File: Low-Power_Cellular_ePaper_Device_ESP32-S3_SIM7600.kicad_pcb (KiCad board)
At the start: 4 copper layers, 85 x 57.5 mm, 100 parts, among them J1 USB_C_Receptacle_GCT_USB4085, J2 JST_PH_S2B-PH-K_1x02_P2.00mm_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, J3 nanoSIM_GCT_SIM8060-6-0-14-00, J4 U.FL_Hirose_U.FL-R-SMT-1_Vert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, J5 U.FL_Hirose_U.FL-R-SMT-1_Vert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, J6 Hirose_FH12-24S-0.5SH_1x24-1M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, J7 JST_SH_SM04B-SRSS-TB_1x04-1MP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, Q1 SOT-23, Q10 SOT-23, Q2 SOT-23, Q3 SOT-23, Q4 SOT-23, Q6 SOT-23, Q7 SOT-23, Q8 SOT-23, Q9 SOT-23, SW1 SW_Push_SPST_NO_Alps_SKRK, SW2 SW_Push_SPST_NO_Alps_SKRK, U1 ESP32-S3-WROOM-1, U2 SIMCom_SIM7600G, U3 SOIC-14_3.9x8.7mm_P1.27mm, U4 SOT-23-5, U5 SOT-23-5, U6 Sensirion_DFN-4_1.5x1.5mm_P0.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

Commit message: Repair CAD metadata and document blocking electrical review findings
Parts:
- C1, C2: value C_0805_2012Metric -> 4.7uF
- C10, C17, C18, C21, C22, C37, C5, C9: value C_0402_1005Metric -> 0.1uF
- C11, C12: value CP_EIA-7343-31_Kemet-D -> 220uF 6.3V ESR35mR
- C13, C14: value C_0805_2012Metric -> 47uF 10V
- C15, C16: value C_0603_1608Metric -> 10uF
- C19: value C_0402_1005Metric -> 33pF
- C20, C29: value C_0603_1608Metric -> 1uF
- C23, C24, C30, C34, C6: value C_0402_1005Metric -> 100nF
- C25, C26, C27, C28: value C_0805_2012Metric -> 4.7uF 25V
- C3, C4, C7, C8: value C_0805_2012Metric -> 10uF
- C31, C32: value C_0402_1005Metric -> DNP
- C33: value C_0402_1005Metric -> 47pF
- C35: value C_0805_2012Metric -> 1uF 25V
- C36: value C_0603_1608Metric -> 1uF 10V
- D1: value D_SMA -> SMAJ5.0A
- D2, D8: value SOT-23-6 -> USBLC6-2SC6
- D3, D4, D5: value D_SOD-123 -> MBR0530
- F1: value Fuse_1206_3216Metric -> 2.5A PTC
- H1, H2, H3, H4: value MountingHole_2.7mm_M2.5_Pad_Via -> M2.5
- J1: value USB_C_Receptacle_GCT_USB4085 -> USB-C
- J2: value JST_PH_S2B-PH-K_1x02_P2.00mm_Horizontal -> BATT (JST-PH)
- J3: value nanoSIM_GCT_SIM8060-6-0-14-00 -> nanoSIM_GCT_SIM8060
- J4: value U.FL_Hirose_U.FL-R-SMT-1_Vertical -> MAIN_ANT_UFL
- J5: value U.FL_Hirose_U.FL-R-SMT-1_Vertical -> GNSS_ANT_UFL
- J6: value Hirose_FH12-24S-0.5SH_1x24-1MP_P0.50mm_Horizontal -> FH12-24S-0.5SH
- J7: value JST_SH_SM04B-SRSS-TB_1x04-1MP_P1.00mm_Horizontal -> Qwiic / STEMMA QT
- L1: value L_0402_1005Metric -> 47nH
- L2: value L_1210_3225Metric -> 10uH 1.2A
- LED1: value LED_0603_1608Metric -> USER (Green)
- LED2: value LED_0603_1608Metric -> NETLIGHT (Yellow)
- LED3: value LED_0603_1608Metric -> CHG (Red)
- Q1, Q6, Q8: value SOT-23 -> AO3401A
- Q10, Q2, Q3, Q4, Q7, Q9: value SOT-23 -> BSS138
- R1, R2: value R_0603_1608Metric -> 5.1k 1%
- R10: value R_0805_2012Metric -> 0.47R 1%
- R11, R20, R3, R4, R9: value R_0603_1608Metric -> 10k
- R12, R18, R7: value R_0603_1608Metric -> 1k
- R13, R14, R15: value R_0402_1005Metric -> 22R
- R16: value R_0402_1005Metric -> 0R
- R17: value R_0603_1608Metric -> 2.0k 1%
- R19, R21, R8: value R_0603_1608Metric -> 100k
- R22, R23: value R_0603_1608Metric -> 4.7k
- R5, R6: value R_0603_1608Metric -> 1M 1%
- SW1: value SW_Push_SPST_NO_Alps_SKRK -> RESET
- SW2: value SW_Push_SPST_NO_Alps_SKRK -> BOOT
- U3: value SOIC-14_3.9x8.7mm_P1.27mm -> TXS0104ED
- U4: value SOT-23-5 -> MCP73831-2-OT
- U5: value SOT-23-5 -> RT9080-33 / AP2112K
- U6: value Sensirion_DFN-4_1.5x1.5mm_P0.8mm_SHT4x_NoCentralPad -> SHT40-AD1B

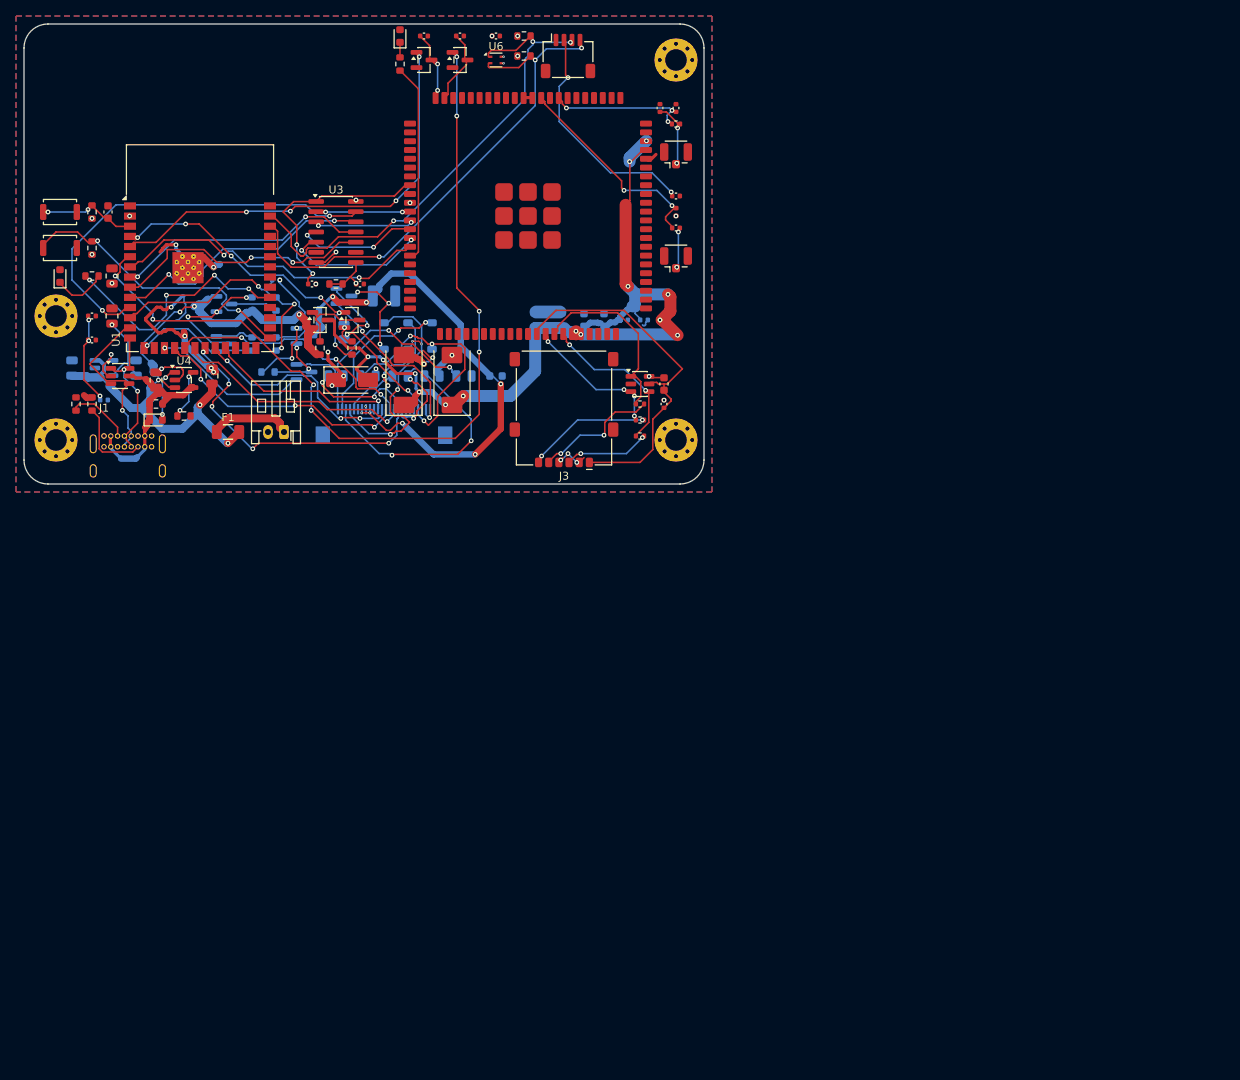
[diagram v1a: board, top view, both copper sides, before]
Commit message: Redesign cellular ePaper revision B and close native CAD connectivity checks
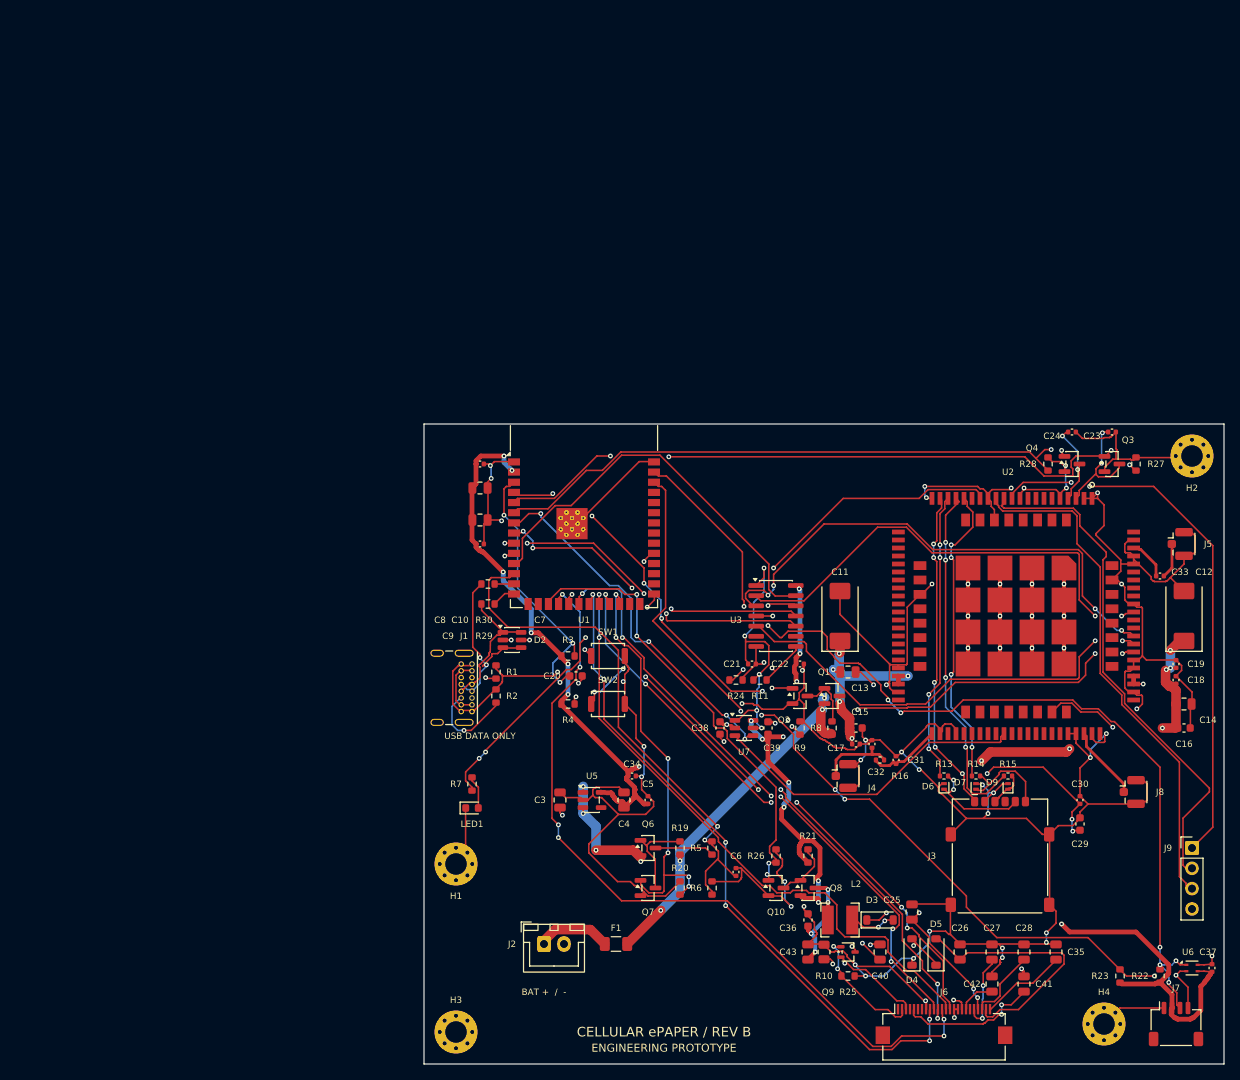
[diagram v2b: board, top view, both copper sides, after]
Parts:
- removed C1, C2: 4.7uF, C_0805_2012Metric
- removed D1: SMAJ5.0A, D_SMA
- removed D8: USBLC6-2SC6, SOT-23-6
- removed L1: 47nH, L_0402_1005Metric
- removed LED2: NETLIGHT (Yellow), LED_0603_1608Metric
- removed LED3: CHG (Red), LED_0603_1608Metric
- removed R12, R18: 1k, R_0603_1608Metric
- removed R17: 2.0k 1%, R_0603_1608Metric
- removed U4: MCP73831-2-OT, SOT-23-5
- added C38: 100nF, Capacitor_SMD:C_0603_1608Metric, F.Cu at (87.0, 88.0)
- added C39: 100nF, Capacitor_SMD:C_0603_1608Metric, F.Cu at (93.0, 88.0)
- added C40: 4.7uF 25V, Capacitor_SMD:C_0805_2012Metric, F.Cu at (107.0, 116.0)
- added C41: 1uF 25V, Capacitor_SMD:C_0805_2012Metric, F.Cu at (125.0, 120.0)
- added C42: 1uF 25V, Capacitor_SMD:C_0805_2012Metric, F.Cu at (121.0, 120.0)
- added C43: 4.7uF 25V, Capacitor_SMD:C_0805_2012Metric, F.Cu at (98.0, 116.0)
- added D6: PESD3V3U1UL, Diode_SMD:D_SOD-882, F.Cu at (115.0, 95.3)
- added D7: PESD3V3U1UL, Cellular:D_SOD-882_SIM, F.Cu at (119.0, 95.3)
- added D9: PESD3V3U1UL, Diode_SMD:D_SOD-882, F.Cu at (123.0, 95.3)
- added J8: LTE diversity, Connector_Coaxial:U.FL_Hirose_U.FL-R-SMT-1_Vertical, F.Cu at (139.0, 96.0)
- added J9: Modem USB service, Connector_PinHeader_2.54mm:PinHeader_1x04_P2.54mm_Vertical, F.Cu at (146.0, 103.0)
- added R24: 100k, Resistor_SMD:R_0603_1608Metric, F.Cu at (89.0, 82.0)
- added R25: 1M, Resistor_SMD:R_0603_1608Metric, F.Cu at (103.0, 119.0)
- added R26: 100k, Resistor_SMD:R_0603_1608Metric, F.Cu at (94.0, 104.0)
- added R27: 100k, Resistor_SMD:R_0603_1608Metric, F.Cu at (139.0, 55.0)
- added R28: 100k, Resistor_SMD:R_0603_1608Metric, F.Cu at (128.0, 55.0)
- added R29: 22R, Resistor_SMD:R_0603_1608Metric, F.Cu at (58.0, 70.0)
- added R30: 22R, Resistor_SMD:R_0603_1608Metric, F.Cu at (58.0, 72.5)
- added U7: SN74LVC1T45DBVR, Package_TO_SOT_SMD:SOT-23-6, F.Cu at (90.0, 88.0)
- C10, C21, C22, C23, C24, C30, C31, C32, C33, C34, C37, C9: footprint C_0402_1005Metric -> Capacitor_SMD:C_0402_1005Metric
- C11, C12: value 220uF 6.3V ESR35mR -> 220uF 6.3V T520D227M006ATE015; footprint CP_EIA-7343-31_Kemet-D -> Capacitor_Tantalum_SMD:CP_EIA-7343-31_Kemet-D
- C13, C14, C3, C35, C4: footprint C_0805_2012Metric -> Capacitor_SMD:C_0805_2012Metric; moved to F.Cu
- C15, C16: footprint C_0603_1608Metric -> Capacitor_SMD:C_0603_1608Metric; moved to F.Cu
- C17, C18, C19, C5, C6: footprint C_0402_1005Metric -> Capacitor_SMD:C_0402_1005Metric; moved to F.Cu
- C20, C29: footprint C_0603_1608Metric -> Capacitor_SMD:C_0603_1608Metric
- C25, C26, C27, C28: value 4.7uF 25V -> 1uF 25V; footprint C_0805_2012Metric -> Capacitor_SMD:C_0805_2012Metric; moved to F.Cu
- C36: value 1uF 10V -> 1uF 25V; footprint C_0603_1608Metric -> Capacitor_SMD:C_0603_1608Metric; moved to F.Cu
- C7, C8: footprint C_0805_2012Metric -> Capacitor_SMD:C_0805_2012Metric
- D2: footprint SOT-23-6 -> Package_TO_SOT_SMD:SOT-23-6
- D3, D4, D5: footprint D_SOD-123 -> Diode_SMD:D_SOD-123; moved to F.Cu
- F1: value 2.5A PTC -> 2.5A fast fuse; footprint Fuse_1206_3216Metric -> Fuse:Fuse_1206_3216Metric
- H1, H2, H3, H4: footprint MountingHole_2.7mm_M2.5_Pad_Via -> MountingHole:MountingHole_2.7mm_M2.5_Pad_Via
- J1: footprint USB_C_Receptacle_GCT_USB4085 -> Cellular:USB4085_Edge
- J2: value BATT (JST-PH) -> Protected LiPo 3A; footprint JST_PH_S2B-PH-K_1x02_P2.00mm_Horizontal -> Connector_JST:JST_XH_B2B-XH-A_1x02_P2.50mm_Vertical
- J3: footprint nanoSIM_GCT_SIM8060-6-0-14-00 -> Connector_Card:nanoSIM_GCT_SIM8060-6-0-14-00
- J4, J5: footprint U.FL_Hirose_U.FL-R-SMT-1_Vertical -> Connector_Coaxial:U.FL_Hirose_U.FL-R-SMT-1_Vertical
- J6: footprint Hirose_FH12-24S-0.5SH_1x24-1MP_P0.50mm_Horizontal -> Connector_FFC-FPC:Hirose_FH12-24S-0.5SH_1x24-1MP_P0.50mm_Horizontal; moved to F.Cu
- J7: footprint JST_SH_SM04B-SRSS-TB_1x04-1MP_P1.00mm_Horizontal -> Connector_JST:JST_SH_SM04B-SRSS-TB_1x04-1MP_P1.00mm_Horizontal
- L2: value 10uH 1.2A -> 47uH SRN4018-470M; footprint L_1210_3225Metric -> Inductor_SMD:L_Bourns-SRN4018; moved to F.Cu
- LED1: footprint LED_0603_1608Metric -> LED_SMD:LED_0603_1608Metric
- Q1, Q2, Q3, Q4: footprint SOT-23 -> Package_TO_SOT_SMD:SOT-23
- Q10, Q6, Q7, Q8: footprint SOT-23 -> Package_TO_SOT_SMD:SOT-23; moved to F.Cu
- Q9: value BSS138 -> Si1308EDL; footprint SOT-23 -> Package_TO_SOT_SMD:SOT-323_SC-70; moved to F.Cu
- R1, R11, R2, R22, R23, R3, R4, R7, R8, R9: footprint R_0603_1608Metric -> Resistor_SMD:R_0603_1608Metric
- R10: value 0.47R 1% -> 2.2R; footprint R_0805_2012Metric -> Resistor_SMD:R_0805_2012Metric; moved to F.Cu
- R13, R14, R15, R16: footprint R_0402_1005Metric -> Resistor_SMD:R_0402_1005Metric
- R19, R20, R21, R5, R6: footprint R_0603_1608Metric -> Resistor_SMD:R_0603_1608Metric; moved to F.Cu
- SW1, SW2: footprint SW_Push_SPST_NO_Alps_SKRK -> Button_Switch_SMD:SW_Push_SPST_NO_Alps_SKRK
- U1: value ESP32-S3-WROOM-1 -> ESP32-S3-WROOM-1-N8; footprint ESP32-S3-WROOM-1 -> Cellular:ESP32-S3-WROOM-1_Edge
- U2: value SIMCom_SIM7600G -> SIM7600G-H; footprint SIMCom_SIM7600G -> Cellular:SIM7600G_H_135
- U3: footprint SOIC-14_3.9x8.7mm_P1.27mm -> Package_SO:SOIC-14_3.9x8.7mm_P1.27mm
- U5: value RT9080-33 / AP2112K -> AP2112K-3.3TRG1; footprint SOT-23-5 -> Package_TO_SOT_SMD:SOT-23-5; moved to F.Cu
- U6: footprint Sensirion_DFN-4_1.5x1.5mm_P0.8mm_SHT4x_NoCentralPad -> Sensor_Humidity:Sensirion_DFN-4_1.5x1.5mm_P0.8mm_SHT4x_NoCentralPad
- moved C37 146.9 mm to (148.5, 118.0), turned to 90 degrees
- moved U6 143.0 mm to (146.0, 118.0)
- moved J7 142.9 mm to (144.0, 125.0)
- moved R22 141.9 mm to (142.0, 119.0), turned to 90 degrees
- moved R23 137.0 mm to (137.0, 119.0), turned to 90 degrees
- moved Q9 103.4 mm to (103.0, 116.0)
- moved C26 103.2 mm to (117.0, 116.0), turned to 90 degrees
- moved C27 103.2 mm to (121.0, 116.0), turned to 90 degrees
- moved C28 103.2 mm to (125.0, 116.0), turned to 90 degrees
- moved C35 103.2 mm to (129.0, 116.0), turned to 90 degrees
- moved J6 102.6 mm to (115.0, 125.0), turned to 0 degrees
- moved H3 102.5 mm to (54.0, 126.0)
- moved Q3 99.7 mm to (136.0, 55.0)
- moved D4 99.5 mm to (111.0, 116.0)
- moved D5 99.5 mm to (114.0, 116.0)
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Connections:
- net EPD_VSH renamed EPD_VSH1
- C25 pad 1: EPD_VGH -> EPD_PREVGH
- C26 pad 1: EPD_VGL -> EPD_PREVGL
- D3 pad 1: EPD_SW -> EPD_PREVGH
- D3 pad 2: EPD_PREVGH -> EPD_SW
- D4 pad 1: EPD_PREVGH -> GND
- D4 pad 2: EPD_VGH -> EPD_FLY
- D5 pad 1: EPD_VGL -> EPD_FLY
- J1 pad A8: (no net) -> unconnected-(J1-SBU1-PadA8)
- J1 pad B8: (no net) -> unconnected-(J1-SBU2-PadB8)
- J3 pad 6: GND -> unconnected-(J3-VPP-Pad6)
- J6 pad 1: (no net) -> unconnected-(J6-Pin_1-Pad1)
- J6 pad 18: VCC_EPD -> EPD_VDD
- J6 pad 19: (no net) -> unconnected-(J6-Pin_19-Pad19)
- J6 pad 4: EPD_VGL -> unconnected-(J6-Pin_4-Pad4)
- J6 pad 5: EPD_VGH -> EPD_VSH2
- J6 pad 6: (no net) -> unconnected-(J6-Pin_6-Pad6)
- J6 pad 7: (no net) -> unconnected-(J6-Pin_7-Pad7)
- LED1 pad 1: USER_LED_R -> GND
- LED1 pad 2: GND -> USER_LED_R
- R11 pad 1: +3.3V -> VDD_EXT
- R11 pad 2: +3.3V -> UART_OE
- U1 pad 13: USB_D- -> MCU_USB_D-
- U1 pad 14: USB_D+ -> MCU_USB_D+
- U1 pad 15: BAT_SENSE_EN -> unconnected-(U1-IO3-Pad15)
- U1 pad 16: (no net) -> unconnected-(U1-IO46-Pad16)
- U1 pad 24: (no net) -> BAT_SENSE_EN
- U1 pad 25: (no net) -> unconnected-(U1-IO48-Pad25)
- U1 pad 26: (no net) -> unconnected-(U1-IO45-Pad26)
- U1 pad 28: (no net) -> unconnected-(U1-IO35-Pad28)
- U1 pad 29: (no net) -> unconnected-(U1-IO36-Pad29)
- U1 pad 30: (no net) -> unconnected-(U1-IO37-Pad30)
- U1 pad 32: (no net) -> unconnected-(U1-IO39-Pad32)
- U1 pad 33: (no net) -> unconnected-(U1-IO40-Pad33)
- U1 pad 34: (no net) -> unconnected-(U1-IO41-Pad34)
- U1 pad 35: (no net) -> unconnected-(U1-IO42-Pad35)
- U1 pad 36: (no net) -> unconnected-(U1-RXD0-Pad36)
- U1 pad 37: (no net) -> unconnected-(U1-TXD0-Pad37)
- U2 pad 11: MODEM_TXD_1V8 -> MODEM_USB_VBUS
- U2 pad 12: MODEM_RXD_1V8 -> MODEM_USB_D-
- U2 pad 13: MODEM_RTS_1V8 -> MODEM_USB_D+
- U2 pad 14: MODEM_CTS_1V8 -> GND
- U2 pad 15: MODEM_STATUS -> VDD_EXT
- U2 pad 16: NETLIGHT -> unconnected-(U2-USB_ID-Pad16)
- U2 pad 17: (no net) -> USIM_DATA
- U2 pad 18: (no net) -> USIM_RST
- U2 pad 19: (no net) -> USIM_CLK
- U2 pad 2: (no net) -> GND
- U2 pad 20: (no net) -> USIM_VDD
- U2 pad 21: (no net) -> unconnected-(U2-SD_CMD-Pad21)
- U2 pad 22: (no net) -> unconnected-(U2-SD_DATA0-Pad22)
- U2 pad 23: (no net) -> unconnected-(U2-SD_DATA1-Pad23)
- U2 pad 24: (no net) -> unconnected-(U2-SD_DATA2-Pad24)
- U2 pad 25: (no net) -> unconnected-(U2-SD_DATA3-Pad25)
- U2 pad 26: (no net) -> unconnected-(U2-SD_CLK-Pad26)
- U2 pad 27: (no net) -> unconnected-(U2-SDIO_DATA1-Pad27)
- U2 pad 28: (no net) -> unconnected-(U2-SDIO_DATA2-Pad28)
- U2 pad 29: (no net) -> unconnected-(U2-SDIO_CMD-Pad29)
- U2 pad 3: (no net) -> PWRKEY_1V8
- U2 pad 30: (no net) -> unconnected-(U2-SDIO_DATA0-Pad30)
- U2 pad 31: (no net) -> unconnected-(U2-SDIO_DATA3-Pad31)
- U2 pad 32: (no net) -> unconnected-(U2-SDIO_CLK-Pad32)
- U2 pad 33: GND -> unconnected-(U2-GPIO3-Pad33)
- U2 pad 34: USIM_VDD -> unconnected-(U2-GPIO6-Pad34)
- U2 pad 35: USIM_DATA -> unconnected-(U2-HSIC_STROBE-Pad35)
- U2 pad 36: USIM_CLK -> unconnected-(U2-HSIC_DATA-Pad36)
- U2 pad 37: USIM_RST -> GND
- U2 pad 4: (no net) -> RESET_1V8
- U2 pad 41: (no net) -> GND
- U2 pad 42: (no net) -> unconnected-(U2-DBG_TXD-Pad42)
- U2 pad 43: (no net) -> GND
- U2 pad 44: (no net) -> unconnected-(U2-VDD_AUX-Pad44)
- U2 pad 45: (no net) -> unconnected-(U2-ISINK-Pad45)
- U2 pad 46: (no net) -> unconnected-(U2-ADC2-Pad46)
- U2 pad 47: (no net) -> unconnected-(U2-ADC1-Pad47)
- U2 pad 48: (no net) -> unconnected-(U2-SD_DET-Pad48)
- U2 pad 49: (no net) -> MODEM_STATUS_1V8
- U2 pad 50: (no net) -> unconnected-(U2-GPIO43-Pad50)
- U2 pad 51: (no net) -> unconnected-(U2-NETLIGHT-Pad51)
- U2 pad 52: (no net) -> unconnected-(U2-GPIO41-Pad52)
- U2 pad 53: (no net) -> unconnected-(U2-USIM_DET-Pad53)
- U2 pad 54: (no net) -> unconnected-(U2-FLIGHTMODE-Pad54)
- U2 pad 55: (no net) -> unconnected-(U2-SCL-Pad55)
- U2 pad 56: (no net) -> unconnected-(U2-SDA-Pad56)
- U2 pad 57: (no net) -> GND
- U2 pad 58: (no net) -> GND
- U2 pad 59: (no net) -> RF_AUX
- U2 pad 6: (no net) -> unconnected-(U2-SPI_CLK-Pad6)
- U2 pad 60: (no net) -> GND
- U2 pad 66: (no net) -> MODEM_RTS_1V8
- U2 pad 67: (no net) -> MODEM_CTS_1V8
- U2 pad 68: (no net) -> MODEM_RXD_1V8
- U2 pad 69: (no net) -> unconnected-(U2-RI-Pad69)
- U2 pad 7: (no net) -> unconnected-(U2-SPI_MISO-Pad7)
- U2 pad 70: (no net) -> unconnected-(U2-DCD-Pad70)
- U2 pad 71: (no net) -> MODEM_TXD_1V8
- U2 pad 73: RF_MAIN -> unconnected-(U2-PCM_OUT-Pad73)
- U2 pad 74: GND -> unconnected-(U2-PCM_IN-Pad74)
- U2 pad 75: RF_GNSS -> unconnected-(U2-PCM_SYNC-Pad75)
- U2 pad 76: GND -> unconnected-(U2-PCM_CLK-Pad76)
- U2 pad 78: (no net) -> GND
- U2 pad 79: (no net) -> RF_GNSS
- U2 pad 8: VDD_EXT -> unconnected-(U2-SPI_MOSI-Pad8)
- U2 pad 81: (no net) -> GND
- U2 pad 82: (no net) -> RF_MAIN
- U2 pad 83: (no net) -> unconnected-(U2-COEX1-Pad83)
- U2 pad 84: (no net) -> unconnected-(U2-COEX2-Pad84)
- U2 pad 85: (no net) -> unconnected-(U2-USB_BOOT-Pad85)
- U2 pad 86: RESET_1V8 -> unconnected-(U2-COEX3-Pad86)
- U2 pad 87: PWRKEY_1V8 -> unconnected-(U2-GPIO77-Pad87)
- U2 pad 88: GND -> unconnected-(U2-RESERVED-Pad88)
- U2 pad 89: GND -> unconnected-(U2-RESERVED-Pad89)
- U2 pad 9: (no net) -> unconnected-(U2-SPI_CS-Pad9)
- U2 pad 90: GND -> unconnected-(U2-RESERVED-Pad90)
- U2 pad 91: GND -> unconnected-(U2-RESERVED-Pad91)
- U2 pad 92: GND -> unconnected-(U2-RESERVED-Pad92)
- U2 pad 94: GND -> unconnected-(U2-GPIO4-Pad94)
- U2 pad 95: GND -> unconnected-(U2-GPIO2-Pad95)
- U2 pad 96: GND -> unconnected-(U2-GPIO1-Pad96)
- U3 pad 6: (no net) -> unconnected-(U3-NC-Pad6)
- U3 pad 8: +3.3V -> UART_OE
- U3 pad 9: (no net) -> unconnected-(U3-NC-Pad9)
- U5 pad 4: (no net) -> unconnected-(U5-NC-Pad4)
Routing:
- net GND: track 115.0 -> 664.0 mm, vias 29 -> 63
- net +3.3V: track 67.0 -> 212.3 mm, vias 19 -> 18
- net MODEM_USB_VBUS: track 0.00 -> 67.8 mm, vias 0 -> 2
- net EPD_CS: track 32.7 -> 96.6 mm, vias 3 -> 6
- net MODEM_USB_D-: track 0.00 -> 63.4 mm
- net MODEM_USB_D+: track 0.00 -> 63.1 mm
- net I2C_SDA: track 61.8 -> 121.7 mm, vias 3 -> 8
- net MODEM_RXD_1V8: track 12.0 -> 64.4 mm, vias 2 -> 4
- net EPD_SCK: track 26.3 -> 78.8 mm, vias 3 -> 2
- net EPD_MOSI: track 22.6 -> 73.1 mm, vias 1 -> 6
- net EPD_DC: track 30.8 -> 78.1 mm, vias 3 -> 6
- net MODEM_TXD_1V8: track 11.4 -> 58.3 mm
- net EPD_RST: track 29.9 -> 75.6 mm, vias 1 -> 6
- net EPD_BUSY: track 37.9 -> 83.5 mm, vias 5 -> 6
- net I2C_SCL: track 64.9 -> 110.3 mm, vias 3 -> 6
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- removed copper zone on In2.Cu, net +3.3V
- removed copper zone on B.Cu, net GND
- removed copper zone on F.Cu, net GND
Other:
- board size 85 x 57.5 mm -> 100 x 80 mm
- board text added: "BAT + / -"
- board text added: "CELLULAR ePAPER / REV B"
- board text added: "ENGINEERING PROTOTYPE"
- board text added: "USB DATA ONLY"
